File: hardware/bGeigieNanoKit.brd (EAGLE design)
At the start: 54.6 x 51.7 mm, 4 parts

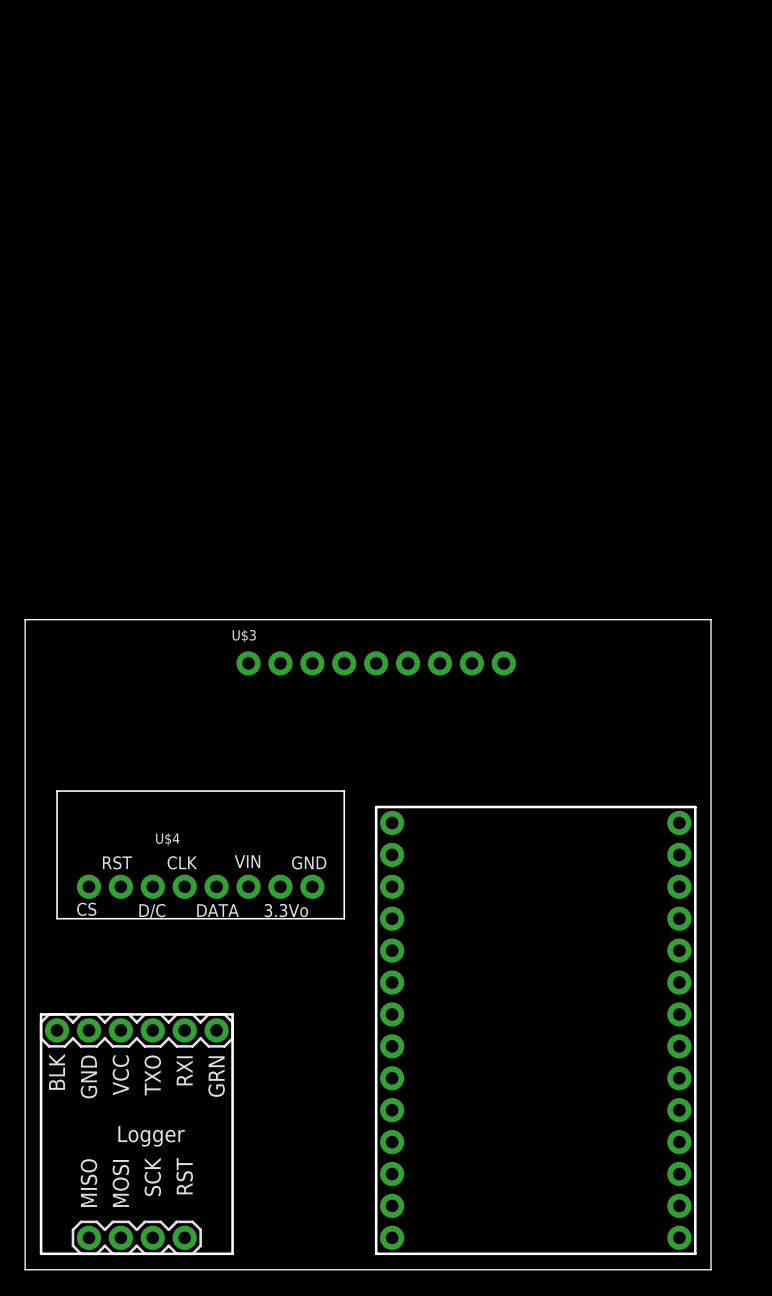
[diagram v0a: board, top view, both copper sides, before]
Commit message: updated hardware files using auto generated footprints
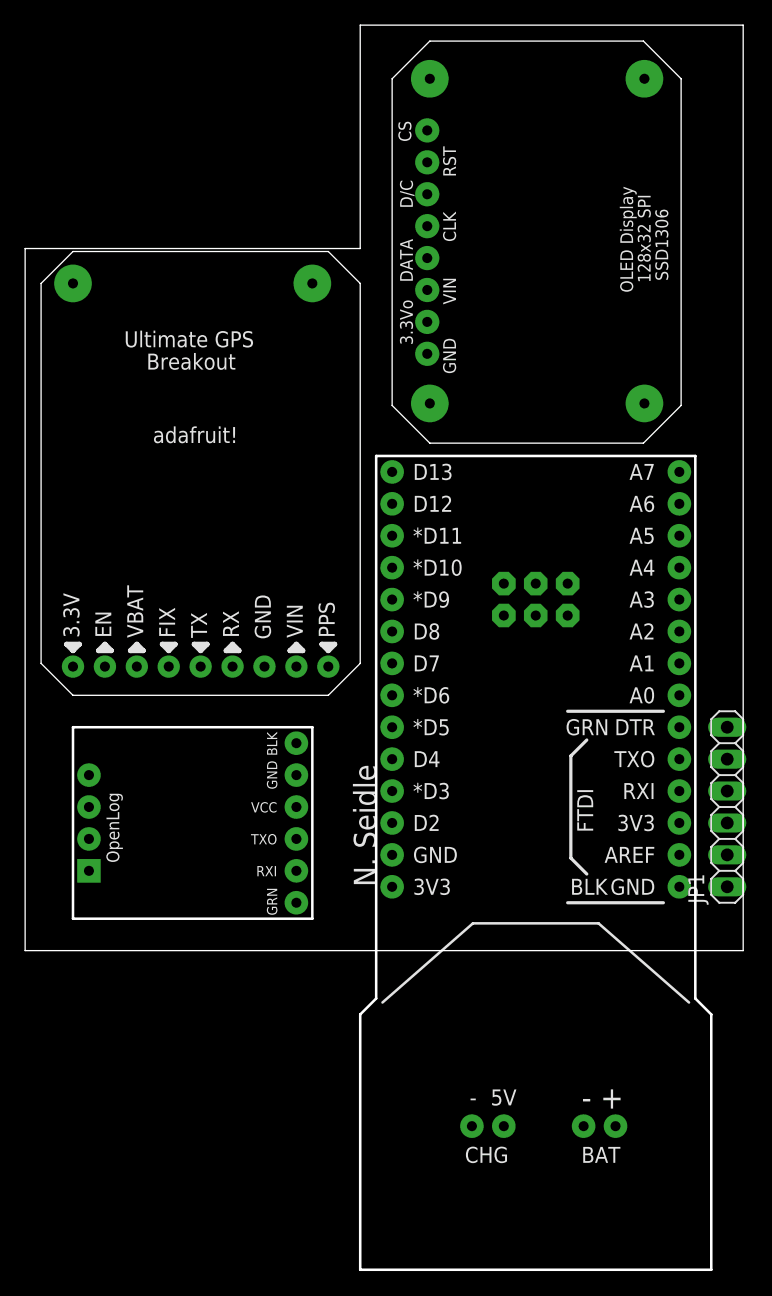
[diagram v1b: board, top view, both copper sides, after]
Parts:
- added JP1: (no value), pinhead:1X06
- U$1: value OPENLOG -> OPENLOGTEST; device open_hw_sockets:OPENLOG -> open_hw_sockets:TEST_OPENLOG
- U$2: value FIO_SOCKET -> FIO_SOCKETTEST; device open_hw_sockets:FIO_SOCKET -> open_hw_sockets:TEST_FIO
- U$3: value ULTIMATE_GPS -> ULTIMATE_GPSTEST; device open_hw_sockets:ULTIMATE_GPS -> open_hw_sockets:TEST_GPS
- U$4: value LCD_SOCKET -> LCD_SOCKETTEST; device open_hw_sockets:LCD_SOCKET -> open_hw_sockets:TEST_LCD
- moved U$4 69.0 mm to (29.2, 97.8), turned to 270 degrees
- moved U$2 47.5 mm to (27.9, 64.8), flipped to the bottom, turned to 180 degrees
- moved U$3 23.0 mm to (1.27, 45.7)
- moved U$1 16.6 mm to (22.9, 27.9), turned to 90 degrees
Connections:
- removed net 3V3: U$2.3V3@2
- new net N$11: JP1.1, U$2.JP5$1
- new net N$12: JP1.2, U$2.JP5$2
- new net N$13: JP1.3, U$2.JP5$3
- new net N$14: JP1.4, U$2.JP5$4
- new net N$15: JP1.5, U$2.JP5$5
- new net N$16: JP1.6, U$2.JP5$6
- net GND: now also U$1.JP1$5, U$1.JP1$6, U$2.JP1$2, U$3.JP1$2, U$3.U$8, U$3.U$9, U$4.U$2, U$4.U$3, U$4.U$4, U$4.U$5; no longer U$1.BLK, U$1.GND, U$2.GND@1, U$2.GND@2, U$3.7
- net N$1: now also U$1.JP1$1, U$2.JP1$13; no longer U$1.GRN, U$2.D12
- net N$10: now also U$2.JP1$5; no longer U$2.D4
- net N$2: now also U$1.JP1$2, U$2.JP1$12; no longer U$1.RXI, U$2.D11
- net N$3: now also U$1.JP1$3, U$2.JP1$11; no longer U$1.TXO, U$2.D10
- net N$4: now also U$2.JP1$10, U$3.JP1$3; no longer U$2.D9, U$3.6
- net N$5: now also U$2.JP1$9, U$3.JP1$4; no longer U$2.D8, U$3.5
- net N$6: now also U$2.JP1$7; no longer U$2.D6
- net N$7: now also U$2.JP1$8; no longer U$2.D7
- net N$8: now also U$2.JP1$6; no longer U$2.D5
- net N$9: now also U$2.JP1$4; no longer U$2.D3
- net VBAT: now also U$3.JP1$6; no longer U$3.3
- net VCC: now also U$1.JP1$4, U$2.JP1$1, U$3.JP1$8; no longer U$1.VCC, U$2.3V3@1, U$3.1
- net VIN: now also U$3.JP1$1; no longer U$3.8
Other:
- board size 54.6 x 51.7 mm -> 57.1 x 73.7 mm
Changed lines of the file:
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@@
 <board>
 <plain>
-<wire x1="0" y1="0" x2="54.59" y2="0" width="0" layer="20"/>
-<wire x1="54.59" y1="0" x2="54.59" y2="51.74" width="0" layer="20"/>
-<wire x1="54.59" y1="51.74" x2="0" y2="51.74" width="0" layer="20"/>
-<wire x1="0" y1="51.74" x2="0" y2="0" width="0" layer="20"/>
+<wire x1="0" y1="25.4" x2="57.15" y2="25.4" width="0" layer="20"/>
+<wire x1="57.15" y1="25.4" x2="57.15" y2="99.06" width="0" layer="20"/>
+<wire x1="57.15" y1="99.06" x2="26.67" y2="99.06" width="0" layer="20"/>
+<wire x1="26.67" y1="99.06" x2="26.67" y2="81.28" width="0" layer="20"/>
+<wire x1="26.67" y1="81.28" x2="0" y2="81.28" width="0" layer="20"/>
+<wire x1="0" y1="81.28" x2="0" y2="25.4" width="0" layer="20"/>
 </plain>
 <attributes>
@@
 </autorouter>
 <elements>
-<element name="U$1" library="open_hw_sockets" package="OPENLOG" value="OPENLOG" x="8.89" y="19.05" rot="R180"/>
-<element name="U$4" library="open_hw_sockets" package="LCD_SOCKET" value="LCD_SOCKET" x="13.97" y="30.48"/>
-<element name="U$3" library="open_hw_sockets" package="ULTIMATE_GPS" value="ULTIMATE_GPS" x="24.13" y="48.26"/>
-<element name="U$2" library="open_hw_sockets" package="FIO_SOCKET" value="FIO_SOCKET" x="40.64" y="19.05"/>
+<element name="U$1" library="open_hw_sockets" package="TEST_OPENLOG" value="OPENLOGTEST" x="22.86" y="27.94" rot="R90"/>
+<element name="U$4" library="open_hw_sockets" package="TEST_LCD" value="LCD_SOCKETTEST" x="29.21" y="97.79" rot="R270"/>
+<element name="U$3" library="open_hw_sockets" package="TEST_GPS" value="ULTIMATE_GPSTEST" x="1.27" y="45.72"/>
+<element name="U$2" library="open_hw_sockets" package="TEST_FIO" value="FIO_SOCKETTEST" x="27.94" y="64.77" rot="MR180"/>
+<element name="JP1" library="pinhead" package="1X06" value="" x="55.88" y="36.83" rot="R90"/>
 </elements>
 <signals>
 <signal name="VIN">
 <contactref element="U$4" pad="6"/>
-<contactref element="U$3" pad="8"/>
-<wire x1="17.78" y1="30.48" x2="35.56" y2="48.26" width="0" layer="19" extent="1-1"/>
+<contactref element="U$3" pad="JP1$1"/>
+<wire x1="21.59" y1="48.006" x2="32.004" y2="77.98000625" width="0" layer="19" extent="1-1"/>
 </signal>
 <signal name="GND">
-<contactref element="U$1" pad="BLK"/>
-<contactref element="U$1" pad="GND"/>
-<contactref element="U$3" pad="7"/>
+<contactref element="U$1" pad="JP1$6"/>
+<contactref element="U$1" pad="JP1$5"/>
+<contactref element="U$3" pad="JP1$2"/>
 <contactref element="U$4" pad="8"/>
-<contactref element="U$2" pad="GND@1"/>
-<contactref element="U$2" pad="GND@2"/>
-<contactref element="U$2" pad="GND@1"/>
-<wire x1="22.86" y1="30.48" x2="33.02" y2="48.26" width="0" layer="19" extent="1-1"/>
-<wire x1="5.08" y1="19.05" x2="22.86" y2="30.48" width="0" layer="19" extent="1-1"/>
-<wire x1="2.54" y1="19.05" x2="5.08" y2="19.05" width="0" layer="19" extent="1-1"/>
-<wire x1="52.07" y1="35.56" x2="2.54" y2="19.05" width="0" layer="19" extent="1-1"/>
-<wire x1="29.21" y1="33.02" x2="52.07" y2="35.56" width="0" layer="19" extent="1-1"/>
-</signal>
-<signal name="3V3">
-<contactref element="U$2" pad="3V3@2"/>
+<contactref element="U$2" pad="JP1$2"/>
+<contactref element="U$2" pad="JP1$2"/>
+<contactref element="U$4" pad="U$2"/>
+<contactref element="U$4" pad="U$3"/>
+<contactref element="U$4" pad="U$4"/>
+<contactref element="U$4" pad="U$5"/>
+<contactref element="U$3" pad="U$8"/>
+<contactref element="U$3" pad="U$9"/>
+<wire x1="32.20999375" y1="94.79000625" x2="49.289996875" y2="94.79000625" width="0" layer="19" extent="1-1"/>
+<wire x1="22.86" y1="78.502003125" x2="32.20999375" y2="94.79000625" width="0" layer="19" extent="1-1"/>
+<wire x1="32.004" y1="72.90000625" x2="22.86" y2="78.502003125" width="0" layer="19" extent="1-1"/>
+<wire x1="32.20999375" y1="68.950003125" x2="32.004" y2="72.90000625" width="0" layer="19" extent="1-1"/>
+<wire x1="49.289996875" y1="68.950003125" x2="32.20999375" y2="68.950003125" width="0" layer="19" extent="1-1"/>
+<wire x1="3.81" y1="78.502003125" x2="22.86" y2="78.502003125" width="0" layer="19" extent="1-1"/>
+<wire x1="19.05" y1="48.006" x2="32.20999375" y2="68.950003125" width="0" layer="19" extent="1-1"/>
+<wire x1="21.59" y1="41.91" x2="19.05" y2="48.006" width="0" layer="19" extent="1-1"/>
+<wire x1="21.59" y1="39.37" x2="21.59" y2="41.91" width="0" layer="19" extent="1-1"/>
+<wire x1="29.21" y1="33.02" x2="21.59" y2="39.37" width="0" layer="19" extent="1-1"/>
 </signal>
 <signal name="N$1">
-<contactref element="U$1" pad="GRN"/>
-<contactref element="U$2" pad="D12"/>
-<wire x1="29.21" y1="5.08" x2="15.24" y2="19.05" width="0" layer="19" extent="1-1"/>
+<contactref element="U$1" pad="JP1$1"/>
+<contactref element="U$2" pad="JP1$13"/>
+<wire x1="21.59" y1="29.21" x2="29.21" y2="60.96" width="0" layer="19" extent="1-1"/>
 </signal>
 <signal name="N$2">
-<contactref element="U$1" pad="RXI"/>
-<contactref element="U$2" pad="D11"/>
-<wire x1="29.21" y1="7.62" x2="12.7" y2="19.05" width="0" layer="19" extent="1-1"/>
+<contactref element="U$1" pad="JP1$2"/>
+<contactref element="U$2" pad="JP1$12"/>
+<wire x1="21.59" y1="31.75" x2="29.21" y2="58.42" width="0" layer="19" extent="1-1"/>
 </signal>
 <signal name="N$3">
-<contactref element="U$1" pad="TXO"/>
-<contactref element="U$2" pad="D10"/>
-<wire x1="29.21" y1="10.16" x2="10.16" y2="19.05" width="0" layer="19" extent="1-1"/>
+<contactref element="U$1" pad="JP1$3"/>
+<contactref element="U$2" pad="JP1$11"/>
+<wire x1="21.59" y1="34.29" x2="29.21" y2="55.88" width="0" layer="19" extent="1-1"/>
 </signal>
 <signal name="VCC">
-<contactref element="U$1" pad="VCC"/>
-<contactref element="U$3" pad="1"/>
+<contactref element="U$1" pad="JP1$4"/>
+<contactref element="U$3" pad="JP1$8"/>
 <contactref element="U$4" pad="7"/>
-<contactref element="U$2" pad="3V3@1"/>
-<wire x1="20.32" y1="30.48" x2="17.78" y2="48.26" width="0" layer="19" extent="1-1"/>
-<wire x1="7.62" y1="19.05" x2="20.32" y2="30.48" width="0" layer="19" extent="1-1"/>
-<wire x1="29.21" y1="35.56" x2="7.62" y2="19.05" width="0" layer="19" extent="1-1"/>
+<contactref element="U$2" pad="JP1$1"/>
+<wire x1="3.81" y1="48.006" x2="32.004" y2="75.44000625" width="0" layer="19" extent="1-1"/>
+<wire x1="21.59" y1="36.83" x2="3.81" y2="48.006" width="0" layer="19" extent="1-1"/>
+<wire x1="29.21" y1="30.48" x2="21.59" y2="36.83" width="0" layer="19" extent="1-1"/>
 </signal>
 <signal name="N$4">
-<contactref element="U$3" pad="6"/>
-<contactref element="U$2" pad="D9"/>
-<wire x1="29.21" y1="12.7" x2="30.48" y2="48.26" width="0" layer="19" extent="1-1"/>
+<contactref element="U$3" pad="JP1$3"/>
+<contactref element="U$2" pad="JP1$10"/>
+<wire x1="16.51" y1="48.006" x2="29.21" y2="53.34" width="0" layer="19" extent="1-1"/>
 </signal>
 <signal name="N$5">
-<contactref element="U$3" pad="5"/>
-<contactref element="U$2" pad="D8"/>
-<wire x1="29.21" y1="15.24" x2="27.94" y2="48.26" width="0" layer="19" extent="1-1"/>
+<contactref element="U$3" pad="JP1$4"/>
+<contactref element="U$2" pad="JP1$9"/>
+<wire x1="13.97" y1="48.006" x2="29.21" y2="50.8" width="0" layer="19" extent="1-1"/>
 </signal>
 <signal name="N$6">
 <contactref element="U$4" pad="5"/>
-<contactref element="U$2" pad="D6"/>
-<wire x1="29.21" y1="20.32" x2="15.24" y2="30.48" width="0" layer="19" extent="1-1"/>
+<contactref element="U$2" pad="JP1$7"/>
+<wire x1="29.21" y1="45.72" x2="32.004" y2="80.52000625" width="0" layer="19" extent="1-1"/>
 </signal>
 <signal name="N$7">
 <contactref element="U$4" pad="4"/>
-<contactref element="U$2" pad="D7"/>
-<wire x1="29.21" y1="17.78" x2="12.7" y2="30.48" width="0" layer="19" extent="1-1"/>
+<contactref element="U$2" pad="JP1$8"/>
+<wire x1="29.21" y1="48.26" x2="32.004" y2="83.06000625" width="0" layer="19" extent="1-1"/>
 </signal>
 <signal name="N$8">
 <contactref element="U$4" pad="3"/>
-<contactref element="U$2" pad="D5"/>
-<wire x1="29.21" y1="22.86" x2="10.16" y2="30.48" width="0" layer="19" extent="1-1"/>
+<contactref element="U$2" pad="JP1$6"/>
+<wire x1="29.21" y1="43.18" x2="32.004" y2="85.60000625" width="0" layer="19" extent="1-1"/>
 </signal>
 <signal name="N$9">
 <contactref element="U$4" pad="2"/>
-<contactref element="U$2" pad="D3"/>
-<wire x1="29.21" y1="27.94" x2="7.62" y2="30.48" width="0" layer="19" extent="1-1"/>
+<contactref element="U$2" pad="JP1$4"/>
+<wire x1="29.21" y1="38.1" x2="32.004" y2="88.14000625" width="0" layer="19" extent="1-1"/>
 </signal>
 <signal name="N$10">
 <contactref element="U$4" pad="1"/>
-<contactref element="U$2" pad="D4"/>
-<wire x1="29.21" y1="25.4" x2="5.08" y2="30.48" width="0" layer="19" extent="1-1"/>
+<contactref element="U$2" pad="JP1$5"/>
+<wire x1="29.21" y1="40.64" x2="32.004" y2="90.68000625" width="0" layer="19" extent="1-1"/>
 </signal>
 <signal name="VBAT">
-<contactref element="U$3" pad="3"/>
+<contactref element="U$3" pad="JP1$6"/>
+</signal>
+<signal name="N$11">
+<contactref element="U$2" pad="JP5$1"/>
+<contactref element="JP1" pad="1"/>
+<wire x1="55.88" y1="30.48" x2="52.07" y2="30.48" width="0" layer="19" extent="1-1"/>
+</signal>
+<signal name="N$12">
+<contactref element="U$2" pad="JP5$2"/>
+<contactref element="JP1" pad="2"/>
+<wire x1="55.88" y1="33.02" x2="52.07" y2="33.02" width="0" layer="19" extent="1-1"/>
+</signal>
+<signal name="N$13">
+<contactref element="U$2" pad="JP5$3"/>
+<contactref element="JP1" pad="3"/>
+<wire x1="55.88" y1="35.56" x2="52.07" y2="35.56" width="0" layer="19" extent="1-1"/>
+</signal>
+<signal name="N$14">
+<contactref element="U$2" pad="JP5$4"/>
+<contactref element="JP1" pad="4"/>
+<wire x1="55.88" y1="38.1" x2="52.07" y2="38.1" width="0" layer="19" extent="1-1"/>
+</signal>
+<signal name="N$15">
+<contactref element="U$2" pad="JP5$5"/>
+<contactref element="JP1" pad="5"/>
+<wire x1="55.88" y1="40.64" x2="52.07" y2="40.64" width="0" layer="19" extent="1-1"/>
+</signal>
+<signal name="N$16">
+<contactref element="U$2" pad="JP5$6"/>
+<contactref element="JP1" pad="6"/>
+<wire x1="55.88" y1="43.18" x2="52.07" y2="43.18" width="0" layer="19" extent="1-1"/>
 </signal>
 </signals>
